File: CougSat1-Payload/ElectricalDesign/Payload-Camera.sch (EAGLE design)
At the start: 63 parts, among them J1 CougSat Card, U1 AD7291, U2 AD8515, U3 AD8616, U4 AD8515, U5 CD74HC4040M, U6 TPS73250, U7 TPS61220, U8 TCA9535R

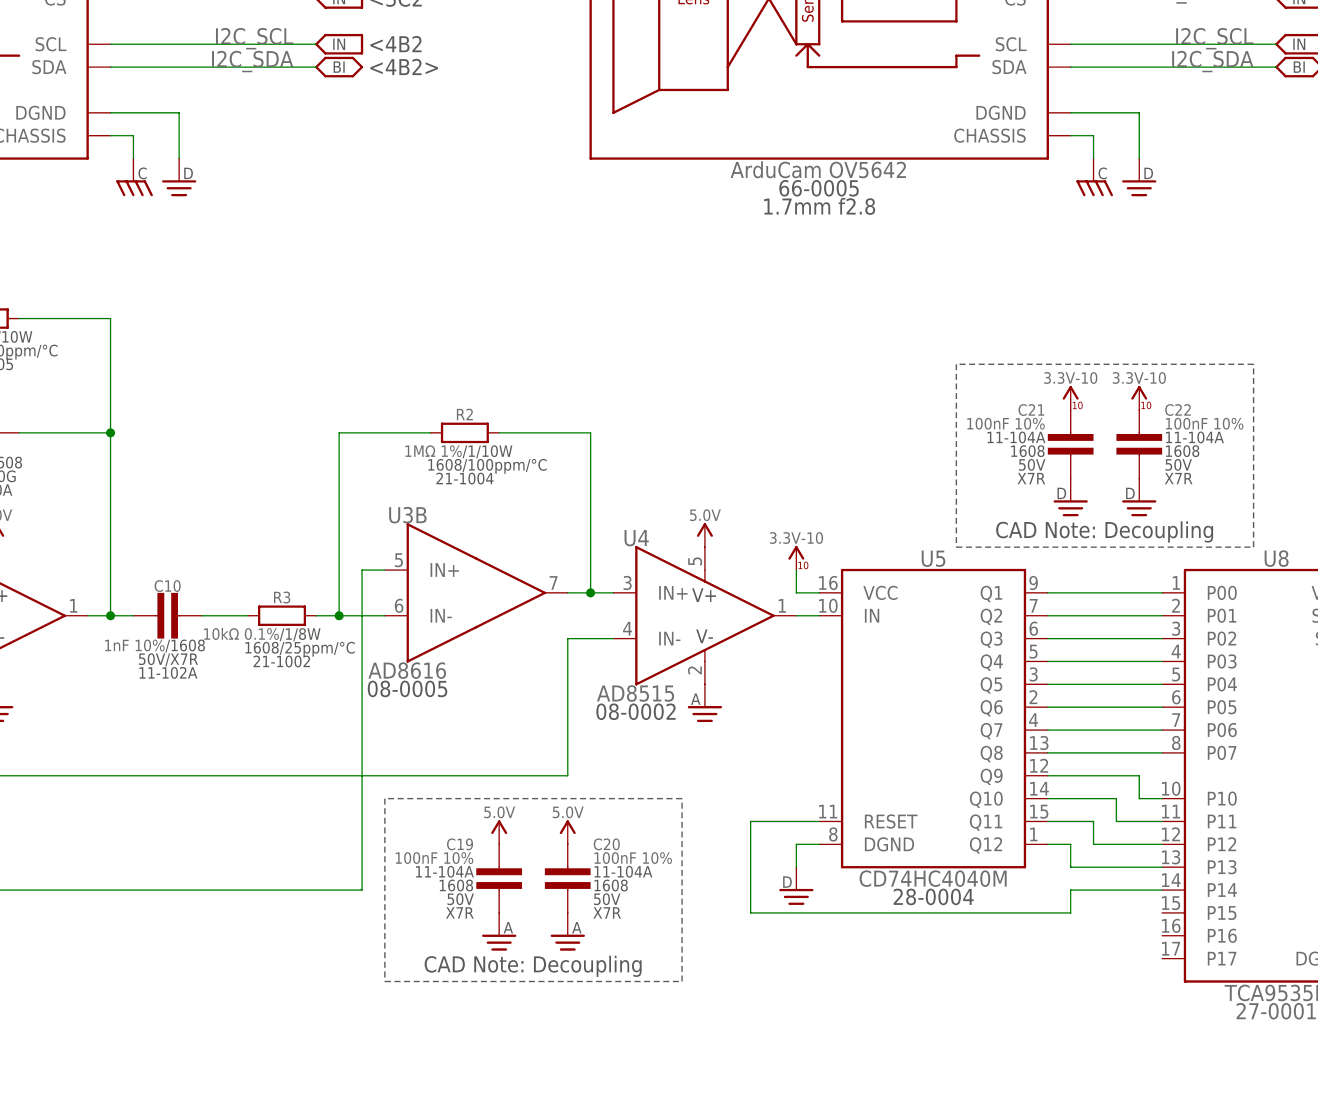
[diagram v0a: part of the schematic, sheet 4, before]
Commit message: Wrote layout constraints
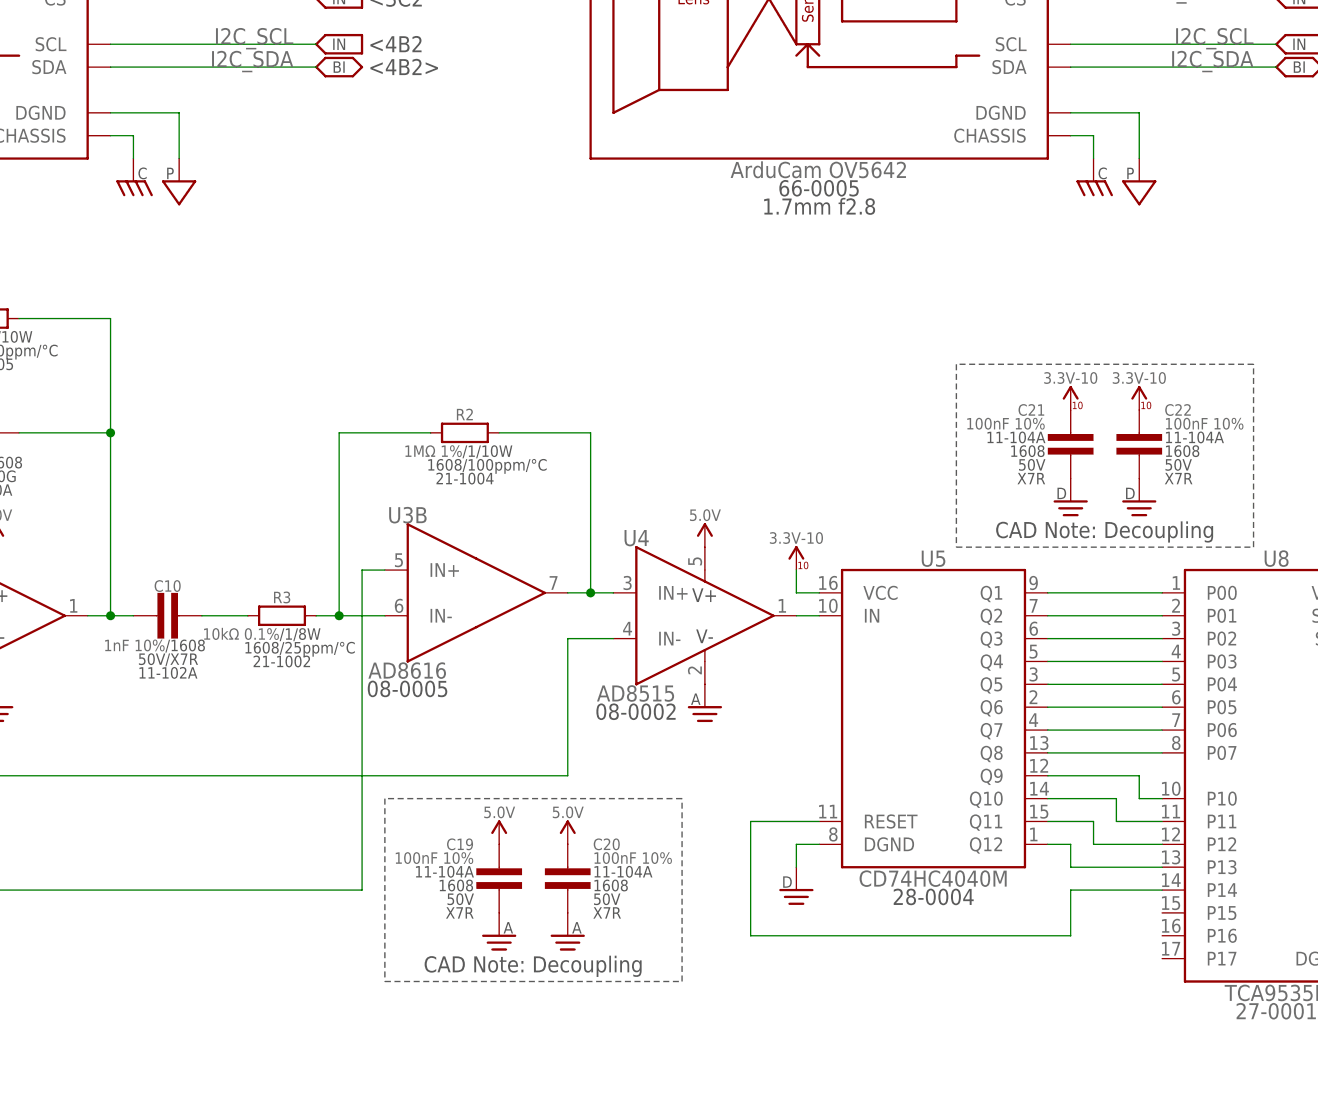
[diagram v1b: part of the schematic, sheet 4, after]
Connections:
- net DGND: no longer B1.DGND, B2.DGND
- net PGND: now also B1.DGND, B2.DGND
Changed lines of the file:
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@@
 <part name="SUPPLY20" library="CougsInSpace-PowerSymbols" deviceset="3.3V-11" device=""/>
 <part name="SUPPLY27" library="CougsInSpace-PowerSymbols" deviceset="3.3V-12" device=""/>
-<part name="SUPPLY30" library="CougsInSpace-PowerSymbols" deviceset="DGND" device=""/>
-<part name="SUPPLY31" library="CougsInSpace-PowerSymbols" deviceset="DGND" device=""/>
 <part name="SUPPLY32" library="CougsInSpace-PowerSymbols" deviceset="CHASSIS" device=""/>
 <part name="SUPPLY33" library="CougsInSpace-PowerSymbols" deviceset="CHASSIS" device=""/>
@@
 <part name="SUPPLY70" library="CougsInSpace-PowerSymbols" deviceset="DGND" device=""/>
 <part name="SUPPLY71" library="CougsInSpace-PowerSymbols" deviceset="3.3V-11" device=""/>
+<part name="SUPPLY30" library="CougsInSpace-PowerSymbols" deviceset="PGND" device=""/>
+<part name="SUPPLY31" library="CougsInSpace-PowerSymbols" deviceset="PGND" device=""/>
 </parts>
 <sheets>
@@
 <attribute name="VALUE" x="177.8" y="166.116" size="1.27" layer="96" rot="MR0" align="center"/>
 </instance>
-<instance part="SUPPLY30" gate="1" x="182.88" y="127" smashed="yes" rot="MR0"/>
-<instance part="SUPPLY31" gate="1" x="76.2" y="127" smashed="yes" rot="MR0"/>
 <instance part="SUPPLY32" gate="G$1" x="71.12" y="127" smashed="yes" rot="MR0"/>
 <instance part="SUPPLY33" gate="G$1" x="177.8" y="127" smashed="yes" rot="MR0"/>
@@
 <attribute name="VALUE" x="187.96" y="181.356" size="1.27" layer="96" align="center"/>
 </instance>
+<instance part="SUPPLY30" gate="G$1" x="76.2" y="127" smashed="yes"/>
+<instance part="SUPPLY31" gate="G$1" x="182.88" y="127" smashed="yes"/>
 </instances>
 <busses>
@@
 </net>
 <net name="DGND" class="0">
-<segment>
-<pinref part="B2" gate="G$1" pin="DGND"/>
-<pinref part="SUPPLY30" gate="1" pin="DGND"/>
-<wire x1="175.26" y1="134.62" x2="182.88" y2="134.62" width="0.1524" layer="91"/>
-<wire x1="182.88" y1="134.62" x2="182.88" y2="129.54" width="0.1524" layer="91"/>
-</segment>
-<segment>
-<pinref part="B1" gate="G$1" pin="DGND"/>
-<pinref part="SUPPLY31" gate="1" pin="DGND"/>
-<wire x1="68.58" y1="134.62" x2="76.2" y2="134.62" width="0.1524" layer="91"/>
-<wire x1="76.2" y1="134.62" x2="76.2" y2="129.54" width="0.1524" layer="91"/>
-</segment>
 <segment>
 <pinref part="U5" gate="G$1" pin="DGND"/>
@@
 <junction x="60.96" y="20.32"/>
 </segment>
+<segment>
+<pinref part="B1" gate="G$1" pin="DGND"/>
+<wire x1="68.58" y1="134.62" x2="76.2" y2="134.62" width="0.1524" layer="91"/>
+<wire x1="76.2" y1="134.62" x2="76.2" y2="129.54" width="0.1524" layer="91"/>
+<pinref part="SUPPLY30" gate="G$1" pin="PGND"/>
+</segment>
+<segment>
+<pinref part="B2" gate="G$1" pin="DGND"/>
+<wire x1="175.26" y1="134.62" x2="182.88" y2="134.62" width="0.1524" layer="91"/>
+<wire x1="182.88" y1="134.62" x2="182.88" y2="129.54" width="0.1524" layer="91"/>
+<pinref part="SUPPLY31" gate="G$1" pin="PGND"/>
+</segment>
 </net>
 <net name="COUNTER_RESET" class="0">
@@
 <pinref part="U8" gate="G$1" pin="P14"/>
 <wire x1="185.42" y1="48.26" x2="175.26" y2="48.26" width="0.1524" layer="91"/>
-<wire x1="175.26" y1="48.26" x2="175.26" y2="45.72" width="0.1524" layer="91"/>
-<wire x1="175.26" y1="45.72" x2="139.7" y2="45.72" width="0.1524" layer="91"/>
+<wire x1="175.26" y1="48.26" x2="175.26" y2="43.18" width="0.1524" layer="91"/>
+<wire x1="175.26" y1="43.18" x2="139.7" y2="43.18" width="0.1524" layer="91"/>
 <pinref part="U5" gate="G$1" pin="RESET"/>
 <wire x1="139.7" y1="55.88" x2="147.32" y2="55.88" width="0.1524" layer="91"/>
-<wire x1="139.7" y1="45.72" x2="139.7" y2="55.88" width="0.1524" layer="91"/>
-</segment>
-</net>
+<wire x1="139.7" y1="43.18" x2="139.7" y2="55.88" width="0.1524" layer="91"/>
+</segment>
+</net>

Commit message: Addressed feedback in schematic section
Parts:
- added U10, U11, U12, U13, U14, U15, U9: TXS0102DQM, CougsInSpace-IC-Comms:LEVEL_SHIFTER-2BIT-XSON-8
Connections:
- net TEMP_0 renamed TEMP_RADIATION_SENSOR
- net TEMP_1 renamed TEMP_5V_REGULATOR
- net TEMP_2 renamed TEMP_CAMERA-0
- net TEMP_3 renamed TEMP_CAMERA-1
- net TEMP_4 renamed TEMP_TOP_LEFT
- net TEMP_5 renamed TEMP_TOP_RIGHT
- net TEMP_6 renamed TEMP_BOTTOM_LEFT
- net TEMP_7 renamed TEMP_BOTTOM_RIGHT
- new net !CS-TELEPHOTO1: U11.A2
- new net !CS-WIDE_ANGLE1: U14.A2
- new net I2C_SCL_CAM0: B1.SCL
- new net I2C_SCL_CAM1: B2.SCL
- new net I2C_SCL_GPIO: U8.SCL
- new net I2C_SDA_CAM0: B1.SDA
- new net I2C_SDA_CAM1: B2.SDA
- new net I2C_SDA_GPIO: U8.SDA
- new net SPI_MISO_CAM0: B1.MISO
- new net SPI_MISO_CAM1: B2.MISO
- new net SPI_MOSI_CAM0: B1.MOSI
- new net SPI_MOSI_CAM1: B2.MOSI
- new net SPI_SCK_CAM0: B1.SCK
- new net SPI_SCK_CAM1: B2.SCK
- net 3.3V_10: now also U1.AS1, U15.OE, U15.VCCA, U15.VCCB, U4.V+
- net 3.3V_11: now also U10.OE, U10.VCCA, U10.VCCB, U11.OE, U11.VCCA, U11.VCCB, U9.OE, U9.VCCA, U9.VCCB
- net 3.3V_12: now also U12.OE, U12.VCCA, U12.VCCB, U13.OE, U13.VCCA, U13.VCCB, U14.OE, U14.VCCA, U14.VCCB
- net 5.0V: no longer U4.V+
- net DGND: now also R10.2, R13.2, U10.DGND, U11.DGND, U12.DGND, U13.DGND, U14.DGND, U15.DGND, U8.A0, U8.A1, U8.A2, U9.DGND; no longer R10.1
- net I2C_SCL: now also U12.A2, U15.A2, U9.A2; no longer B1.SCL, B2.SCL, U8.SCL
- net I2C_SDA: now also U12.A1, U15.A1, U9.A1; no longer B1.SDA, B2.SDA, U8.SDA
- net PGND: now also R10.1; no longer R10.2, R13.2
- net SPI_MISO: now also U10.A2, U13.A2; no longer B1.MISO, B2.MISO
- net SPI_MOSI: now also U11.A1, U14.A1; no longer B1.MOSI, B2.MOSI
- net SPI_SCK: now also U10.A1, U13.A1; no longer B1.SCK, B2.SCK
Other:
- note added: "5V Regulator"
- note added: "I2C Address: 0x20"
- note added: "I2C Address: 0x22"

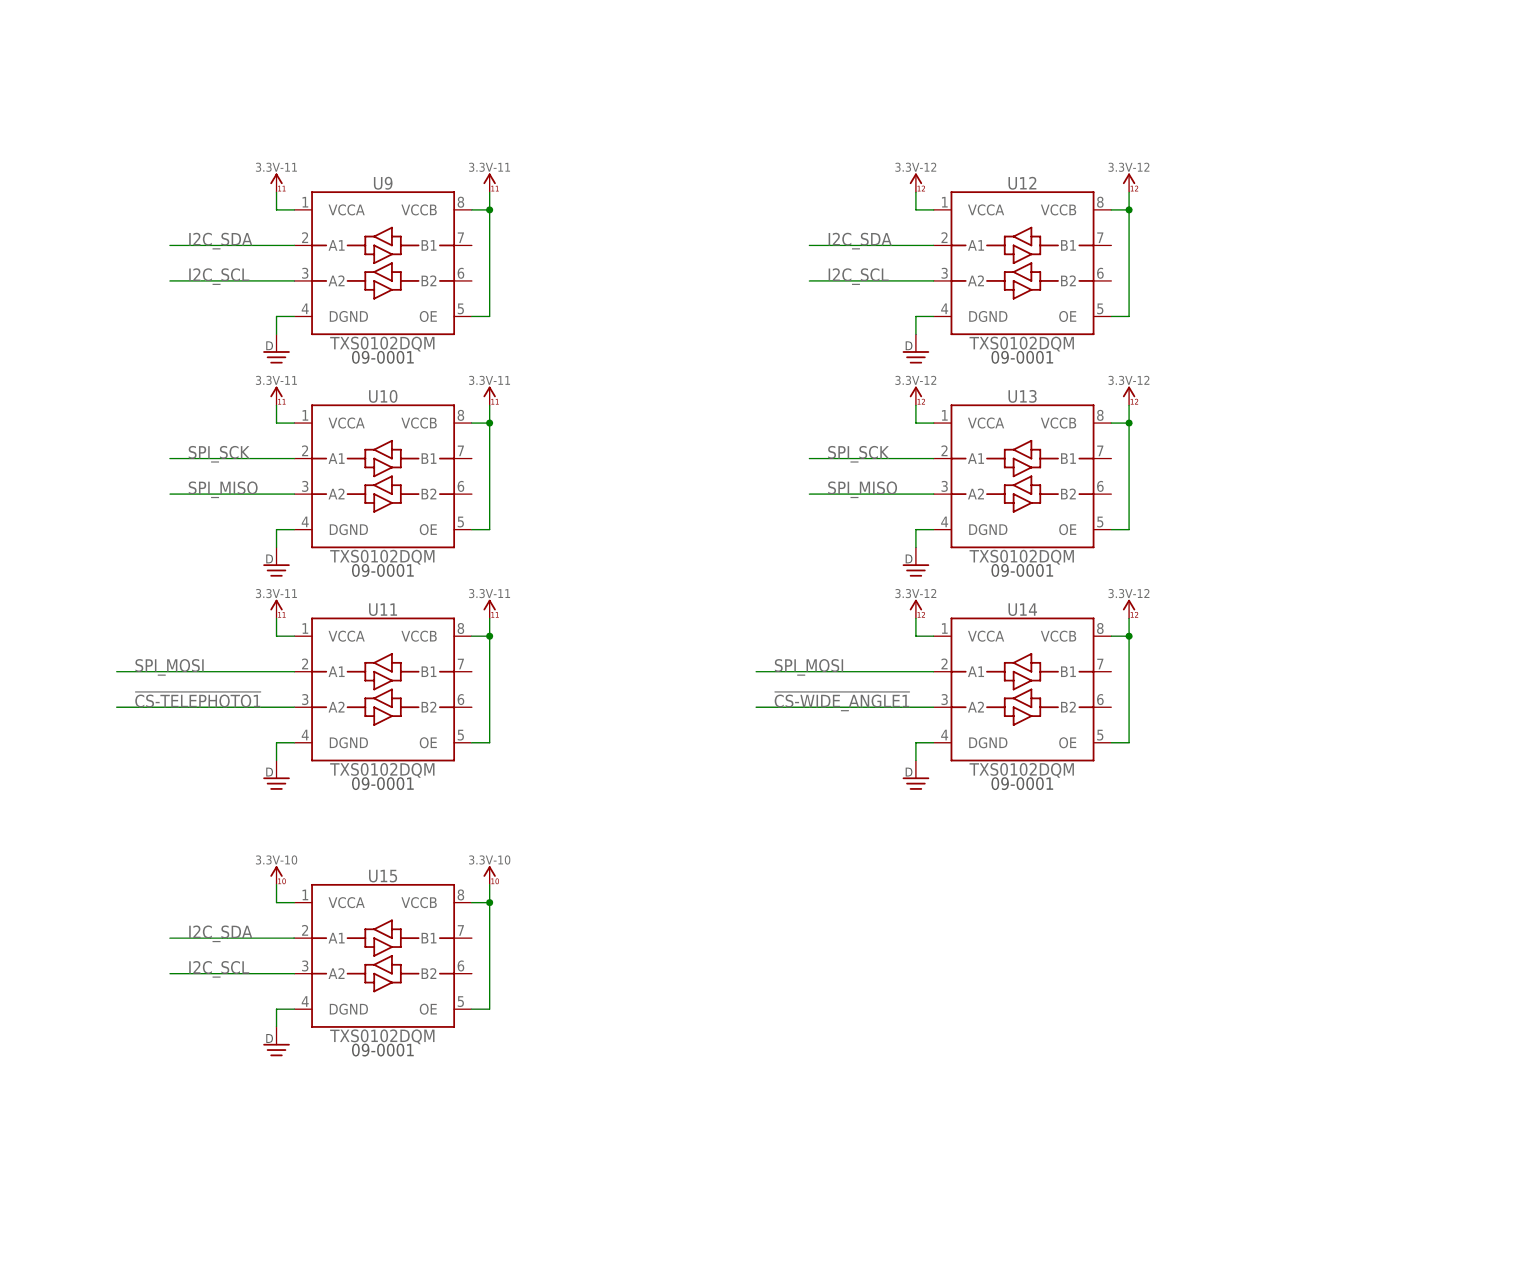
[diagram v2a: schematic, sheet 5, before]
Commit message: Added buffers on I2C and SPI busses
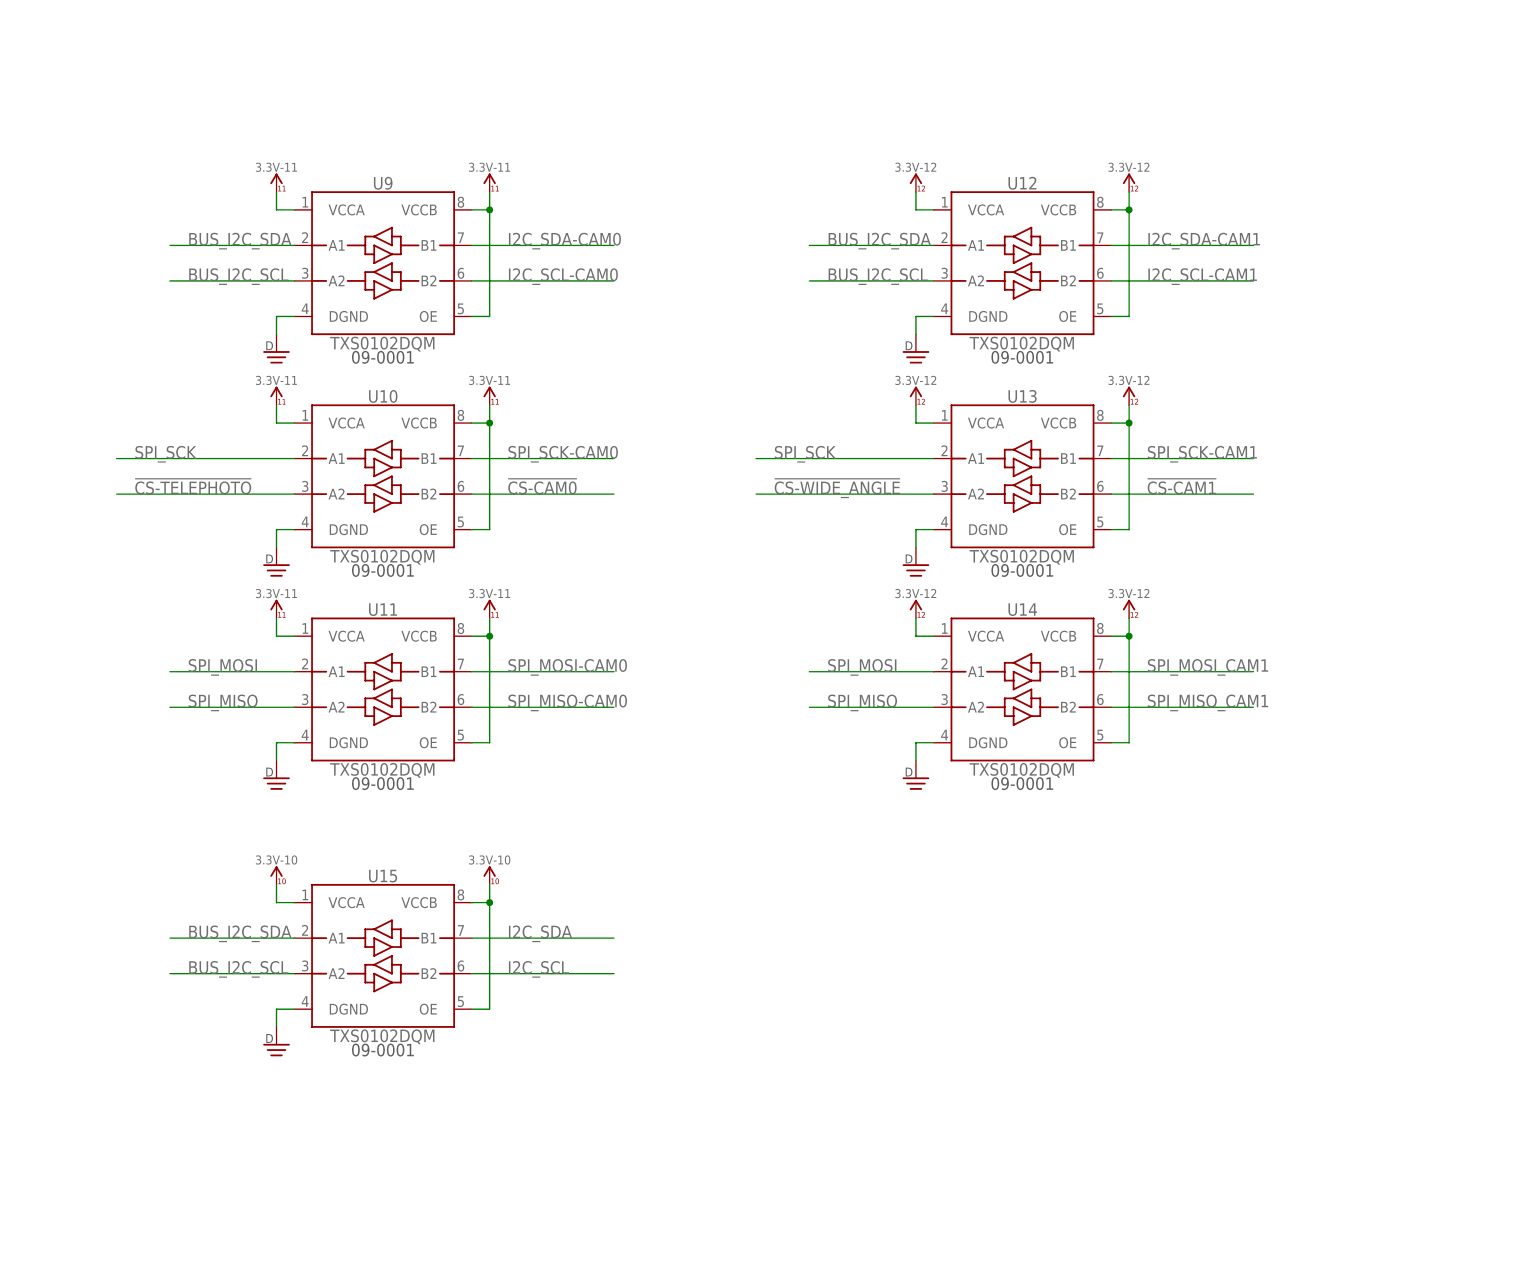
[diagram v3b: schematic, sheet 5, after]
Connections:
- removed net !CS-TELEPHOTO1: U11.A2
- removed net !CS-WIDE_ANGLE1: U14.A2
- removed net I2C_SCL_CAM0: B1.SCL
- removed net I2C_SCL_CAM1: B2.SCL
- removed net I2C_SCL_GPIO: U8.SCL
- removed net I2C_SDA_CAM0: B1.SDA
- removed net I2C_SDA_CAM1: B2.SDA
- removed net I2C_SDA_GPIO: U8.SDA
- removed net SPI_MISO_CAM0: B1.MISO
- removed net SPI_MOSI_CAM0: B1.MOSI
- removed net SPI_SCK_CAM0: B1.SCK
- removed net SPI_SCK_CAM1: B2.SCK
- new net !CS-CAM0: B1.!CS, U10.B2
- new net !CS-CAM1: B2.!CS, U13.B2
- new net BUS_I2C_SCL: J1DATA.BUS_I2C1_SCL, U12.A2, U15.A2, U9.A2
- new net BUS_I2C_SDA: J1DATA.BUS_I2C1_SDA, U12.A1, U15.A1, U9.A1
- new net I2C_SCL-CAM0: B1.SCL, U9.B2
- new net I2C_SCL-CAM1: B2.SCL, U12.B2
- new net I2C_SDA-CAM0: B1.SDA, U9.B1
- new net I2C_SDA-CAM1: B2.SDA, U12.B1
- new net SPI_MISO-CAM0: B1.MISO, U11.B2
- new net SPI_MISO-CAM1: B2.MISO
- new net SPI_MOSI-CAM0: B1.MOSI, U11.B1
- new net SPI_MOSI-CAM1: B2.MOSI
- new net SPI_SCK-CAM0: B1.SCK, U10.B1
- new net SPI_SCK-CAM1: B2.SCK, U13.B1
- net !CS-TELEPHOTO: now also U10.A2; no longer B1.!CS
- net !CS-WIDE_ANGLE: now also U13.A2; no longer B2.!CS
- net I2C_SCL: now also U15.B2, U8.SCL; no longer J1DATA.BUS_I2C1_SCL, U12.A2, U15.A2, U9.A2
- net I2C_SDA: now also U15.B1, U8.SDA; no longer J1DATA.BUS_I2C1_SDA, U12.A1, U15.A1, U9.A1
- net SPI_MISO: now also U11.A2, U14.A2; no longer U10.A2, U13.A2
- net SPI_MISO_CAM1: now also U14.B2; no longer B2.MISO
- net SPI_MOSI_CAM1: now also U14.B1; no longer B2.MOSI

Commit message: Exported PDFs
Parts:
- added H1: Analog Shield, CougsInSpace-Hardware:SHIELDING-2626
- added LOGO1: SIGNATUREHENDRIK, CougsInSpace-Aesthetics:SIGNATUREHENDRIK
- added TP4, TP5: TEST_POINT-THT-1.0, CougsInSpace-Connectors:TEST_POINT-THT-1.0
- B1: device CougsInSpace-Sensors:ARDUCAM-5MP-1.7MM-F2.8 -> CougsInSpace-Sensors:ARDUCAM-5MP-12MM-F2.8
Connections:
- new net 3.3V_0: U10.VCCA, U11.VCCA, U12.VCCA, U13.VCCA, U14.VCCA, U15.VCCA, U9.VCCA
- net 3.3V_10: now also TP5.1; no longer U15.VCCA
- net 3.3V_11: no longer U10.VCCA, U11.VCCA, U9.VCCA
- net 3.3V_12: no longer U12.VCCA, U13.VCCA, U14.VCCA
- net AGND: now also H1.SHIELD
- net PGND: now also TP4.1
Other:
- note added: "3B2>"
- note added: "3C6> 4C6>"
- note added: "4B3>"
- note added: "4B5>"
- note added: "5A1> 5B4> 5C1>"
- note added: "5B1>"
- note added: "5B1> 5B4>"
- note added: "5B4>"
- note added: "5C1> 5C4>"
- note added: "5C3>"
- note added: "5C6>"
- note added: "<3C6> <4C6>"
- note added: "<4A3"
- note added: "<4A5"
- note added: "<4B3>"
- note added: "<4B5>"
- note added: "<5A1> <5B4> <5C1>"
- note added: "<5B3"
- note added: "<5B3>"
- note added: "<5B6"
- note added: "<5B6>"
- note added: "<5C1 <5C4"
- note added: "<5C3"
- note added: "<5C3>"
- note added: "<5C6"
- note removed: "3C6> 4A3> 4A5>"
- note removed: "4A3> 4A5>"
- note removed: "<3B2"
- note removed: "<3C2>"
- note removed: "<3C6> <4A3> <4A5>"
- note removed: "<4A3 <4A5"
- note removed: "<4B2"
- note removed: "<4B2>"
- moved on the sheet: J1JTAG, U10, U12, U13, U14, U9
